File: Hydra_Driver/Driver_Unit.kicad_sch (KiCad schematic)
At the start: 29 parts, among them IC2 DRV8313RHHR, U3 74HC32, U4 INA199xxDCK, U5 INA199xxDCK

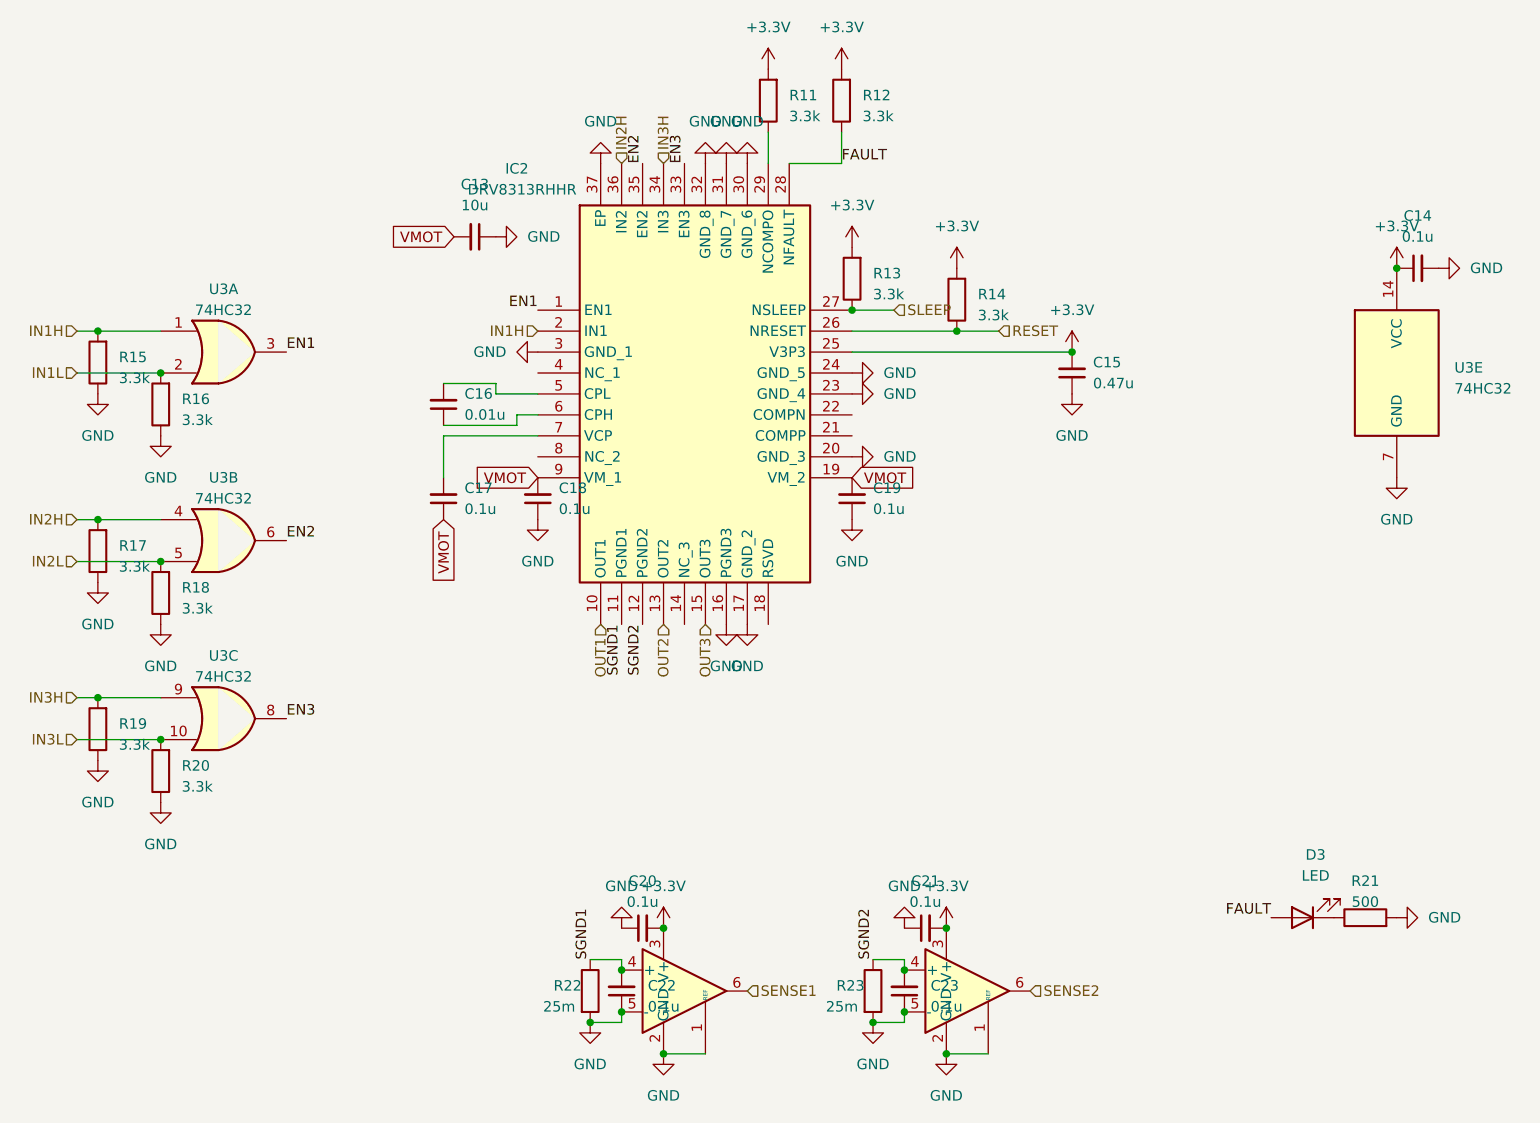
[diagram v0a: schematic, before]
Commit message: Finished general layout of hydra board
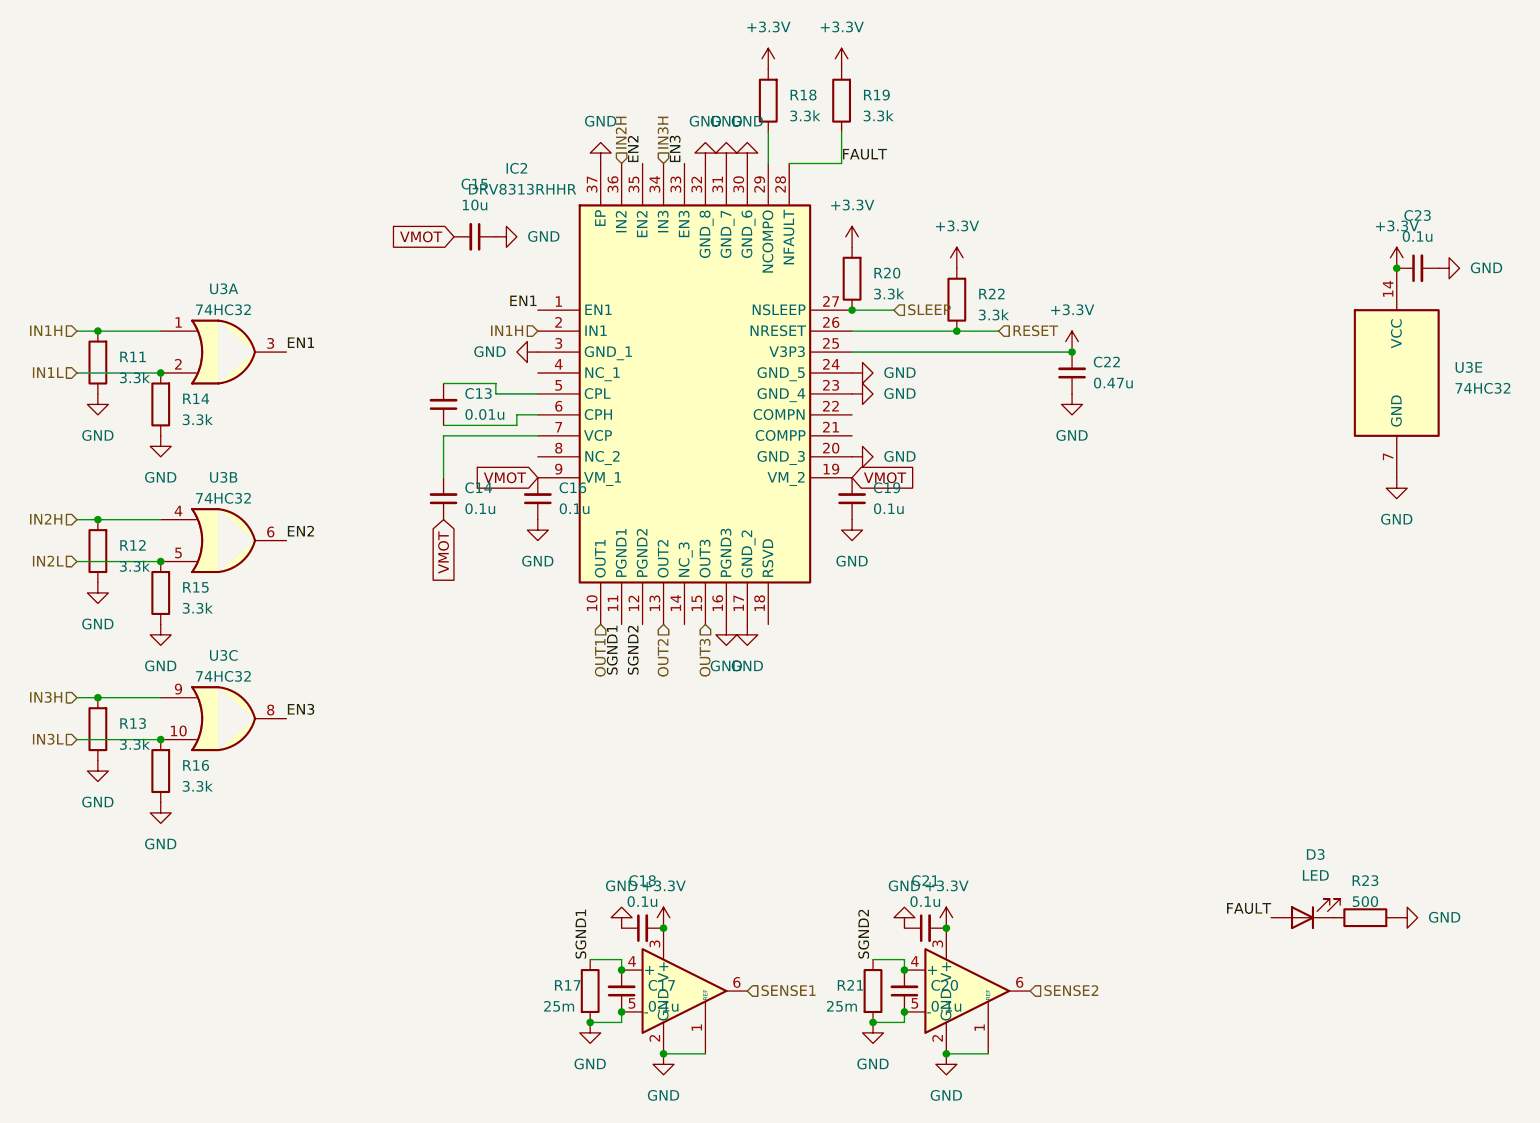
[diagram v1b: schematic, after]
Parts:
- renumbered C16 to C13, C17 to C14, C13 to C15, C18 to C16, C22 to C17, C20 to C18, C23 to C20, C15 to C22, C14 to C23, R15 to R11, R17 to R12, R19 to R13, R16 to R14, R18 to R15, R20 to R16, R22 to R17, R11 to R18, R12 to R19, R13 to R20, R23 to R21, R14 to R22, R21 to R23

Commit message: Component placement mostly finalized
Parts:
- renumbered D3 to D4
